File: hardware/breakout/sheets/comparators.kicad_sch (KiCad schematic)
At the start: 16 parts, among them U54 LM339, U55 MCP4728

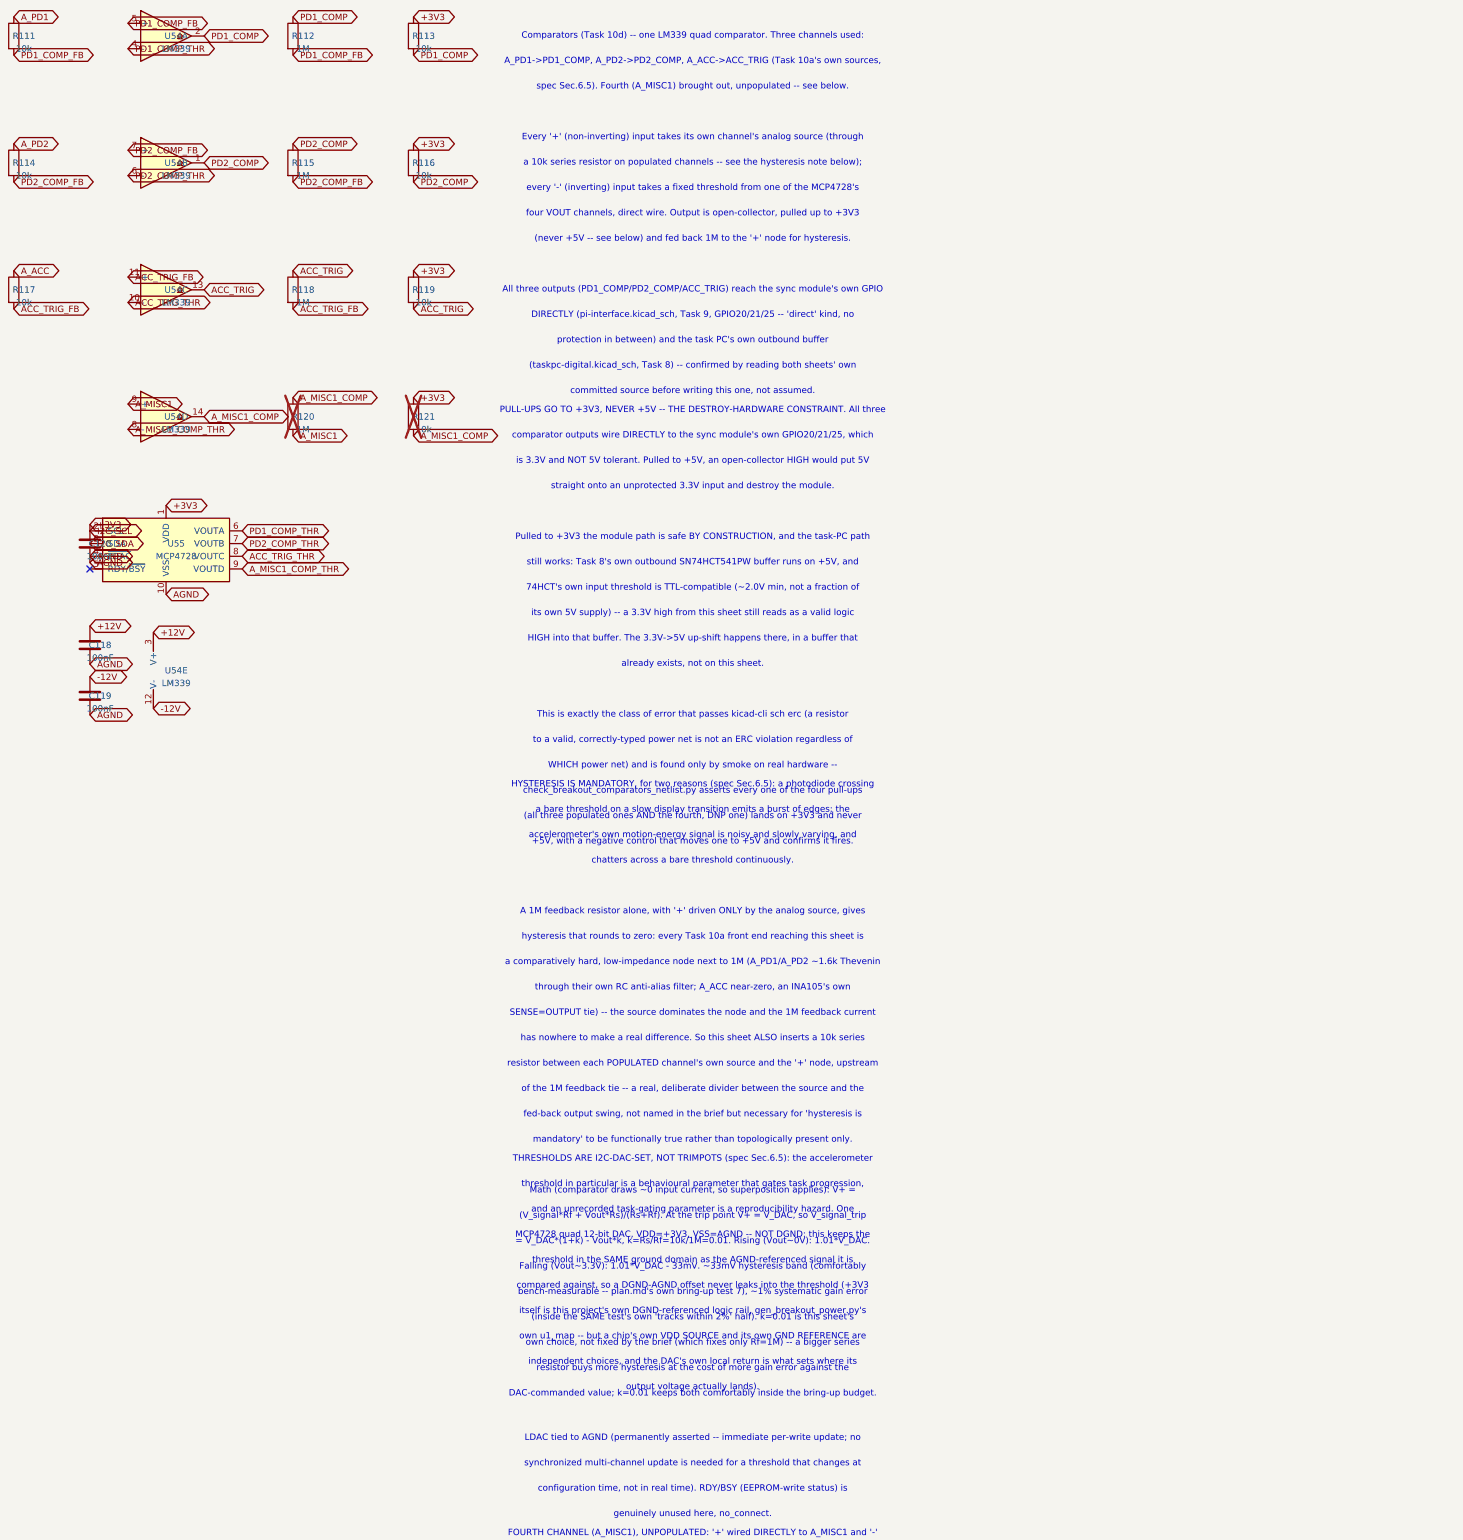
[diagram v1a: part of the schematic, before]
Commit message: fix(hw): run the LM339 from +12V and AGND, never -12V
LM339 pin 12 is labelled "V-"/negative supply, but it is also the common
emitter of all four open-collector output transistors. Whatever pin 12
sits on IS this sheet's output LOW level. On -12V an output LOW is
V- + V_CEsat ~ -11.9V, not 0V, and it genuinely settles there: a 10k
pull-up to +3V3 sources ~0.33mA against a ~16mA sink, so the transistor
stays hard in saturation.

PD1_COMP, PD2_COMP, ACC_TRIG and A_MISC1_COMP carried that level with no
series resistance and no clamp anywhere on the path:

  - J7 pins 38/40/22 (GPIO20/21/25), pad absolute minimum -0.5V. -11.9V
    forward-biases the module's substrate diode at ~1.5mA continuous.
  - U11 pins 2/3/4, SN74HCT541 inputs, absolute minimum -0.5V likewise.
  - U61 pins 6/8, ACSL-6400 LED cathodes with anodes on +5V through 430R:
    I_F ~ 36mA against a 20mA absolute maximum.

It also corrupted the hysteresis silently. The ~33mV band is derived from
a 0->3.3V output swing; the real swing was 15.2V, giving ~150mV and a
~118mV offset from the commanded threshold -- 12% at V_DAC = 1V, against
a 2% bring-up acceptance criterion.

V- = AGND costs nothing. The MCP4728 that sets every threshold is on
+3V3, so thresholds are 0-3.3V; all three populated channels' sources are
AGND-referenced and unipolar-positive; and V+ = +12V still puts the input
common-mode ceiling (10.5V) above anything the front end delivers. The
sheet no longer consumes -12V at all, so its second decoupler moves to
+12V/AGND with it (33/33 -> 34/32 on the power sheet's rail-pair table).
Both decouplers are kept rather than collapsed to one so no reference
designator and no BOM quantity changes, leaving Task 13's committed BOM
and procurement audit valid.

The one caveat, on-sheet as note 6 and in the generator docstring:
A_MISC1 is the only +-5V-capable input reaching this sheet and it is the
DNP fourth channel's '+' source. With V- = AGND that channel can no
longer threshold its input's negative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
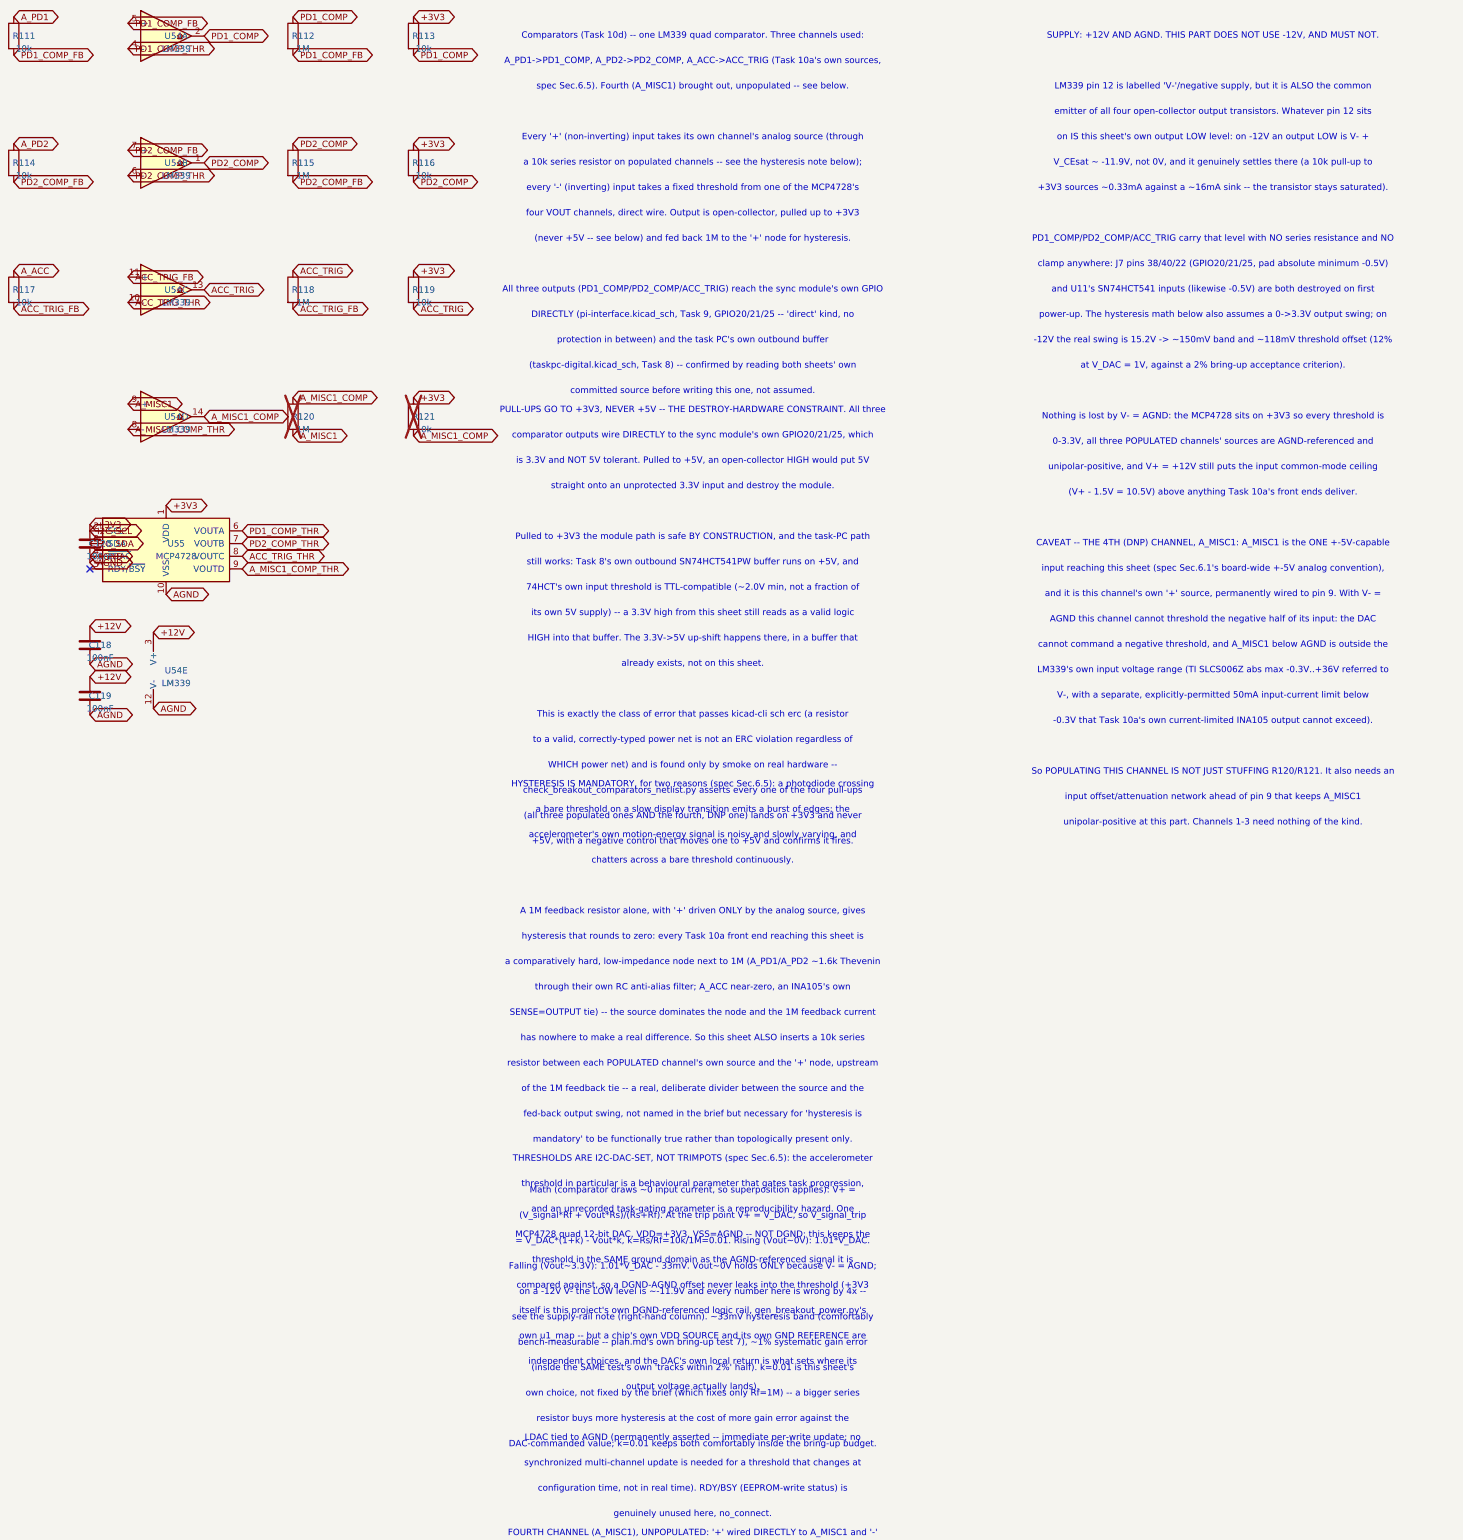
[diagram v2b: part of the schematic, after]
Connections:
- net +12V: now also C119.1
- net AGND: now also U54.12 (V-)
- removed net -12V: C119.1, U54.12 (V-)
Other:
- note added: "(V+ - 1.5V = 10.5V) above anything Task 10a's front ends deliver."
- note added: "+3V3 sources ~0.33mA against a ~16mA sink -- the transistor stays saturated)."
- note added: "-0.3V that Task 10a's own current-limited INA105 output cannot exceed)."
- note added: "-12V the real swing is 15.2V -> ~150mV band and ~118mV threshold offset (12%"
- note added: "0-3.3V, all three POPULATED channels' sources are AGND-referenced and"
- note added: "AGND this channel cannot threshold the negative half of its input: the DAC"
- note added: "CAVEAT -- THE 4TH (DNP) CHANNEL, A_MISC1: A_MISC1 is the ONE +-5V-capable"
- note added: "Falling (Vout~3.3V): 1.01*V_DAC - 33mV. Vout~0V holds ONLY because V- = AGND;"
- note added: "LM339 pin 12 is labelled 'V-'/negative supply, but it is ALSO the common"
- note added: "LM339's own input voltage range (TI SLCS006Z abs max -0.3V..+36V referred to"
- note added: "Nothing is lost by V- = AGND: the MCP4728 sits on +3V3 so every threshold is"
- note added: "PD1_COMP/PD2_COMP/ACC_TRIG carry that level with NO series resistance and NO"
- note added: "SUPPLY: +12V AND AGND. THIS PART DOES NOT USE -12V, AND MUST NOT."
- note added: "So POPULATING THIS CHANNEL IS NOT JUST STUFFING R120/R121. It also needs an"
- note added: "V-, with a separate, explicitly-permitted 50mA input-current limit below"
- note added: "V_CEsat ~ -11.9V, not 0V, and it genuinely settles there (a 10k pull-up to"
- note added: "and U11's SN74HCT541 inputs (likewise -0.5V) are both destroyed on first"
- note added: "and it is this channel's own '+' source, permanently wired to pin 9. With V- ="
- note added: "at V_DAC = 1V, against a 2% bring-up acceptance criterion)."
- note added: "cannot command a negative threshold, and A_MISC1 below AGND is outside the"
- note added: "clamp anywhere: J7 pins 38/40/22 (GPIO20/21/25, pad absolute minimum -0.5V)"
- note added: "emitter of all four open-collector output transistors. Whatever pin 12 sits"
- note added: "input offset/attenuation network ahead of pin 9 that keeps A_MISC1"
- note added: "input reaching this sheet (spec Sec.6.1's board-wide +-5V analog convention),"
- note added: "on IS this sheet's own output LOW level: on -12V an output LOW is V- +"
- note added: "on a -12V V- the LOW level is ~-11.9V and every number here is wrong by 4x --"
- note added: "power-up. The hysteresis math below also assumes a 0->3.3V output swing; on"
- note added: "see the supply-rail note (right-hand column). ~33mV hysteresis band (comfortably"
- note added: "unipolar-positive at this part. Channels 1-3 need nothing of the kind."
- note added: "unipolar-positive, and V+ = +12V still puts the input common-mode ceiling"
- note removed: "Falling (Vout~3.3V): 1.01*V_DAC - 33mV. ~33mV hysteresis band (comfortably"

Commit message: fix(hw): protect comparator channel 4's live A_MISC1 input with a series R
A_MISC1 is a live +-5V net (U28's INA105 output), permanently wired to
U54 pin 9 regardless of this channel's own populate state, and also
fanned out to U34/U36 and every ADG1206 mux's own S14. With V- = AGND
(the prior round's own fix), A_MISC1's negative half sits outside the
LM339's input range on every assembled board -- a bare wire from pin 9
is a standing clamp at the input protection diode's forward drop, with
fault current limited only by the INA105's own current limit, straight
into the LM339's substrate. Channels 1-3 are protected by R111/R114/R117
(10k series); channel 4 had no equivalent.

R190 (10k, populated -- not DNP, unlike this channel's pull-up/feedback)
closes that gap, wired identically to channels 1-3: A_MISC1 -> R190 ->
A_MISC1_COMP_FB -> U54 pin 9. It does not populate the channel in the
sense that matters for thresholding (feedback and pull-up stay DNP), it
only bounds the fault current to ~0.43mA instead of a bare wire.

A prior attempt deferred this because an auto-numbered resistor becomes
comparators.kicad_sch's own new "R" maximum, and opto-ni/opto-intan/
control-usb-i2c all seed their own resistor numbering from it via
find_max_refs(COMPARATORS_SCH) -- renumbering ~66 already-committed
refdes for no functional reason. R190 is placed with an explicit refdes
(two_pin()'s own new `ref=` passthrough, bypassing sch.next_ref("R"))
chosen to sit above the whole board's prior "R" range (189) on purpose,
and the three downstream generators pin their own inherited "R" seed to
its pre-R190 value (121/170/187) rather than re-deriving it from this
sheet's text. Confirmed by regenerating all three in-memory and diffing
their own (ref -> value) map against the committed sheets: zero refs
added, removed, or changed. Diffing the whole board's own component
list (netlist-contract.json) against 52dfcf7 confirms the same at the
board level -- R190 added, nothing else touched.

chec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
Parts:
- added R190: 10k, Resistor_SMD:R_0603_1608Metric, symbol Device:R
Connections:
- net A_MISC1: now also R190.1; no longer R120.2, U54.9 (+)
- new net A_MISC1_COMP_FB: R120.2, R190.2, U54.9 (+)
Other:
- note added: "'-' wired directly to the DAC's own VOUTD -- both real, permanent connections"
- note added: "-0.3V that Task 10a's own current-limited INA105 output cannot exceed). R190"
- note added: "DNP feedback and pull-up still need stuffing, AND (module docstring / note 6)"
- note added: "FOURTH CHANNEL (A_MISC1): '+' reaches A_MISC1 through R190 (10k, POPULATED),"
- note added: "R190 (10k, POPULATED -- see the fourth-channel note, left column). With V- ="
- note added: "R190 IS POPULATED, UNLIKE THE PULL-UP/FEEDBACK, BECAUSE A_MISC1 IS LIVE: it is"
- note added: "R190 does not by itself make this channel a working threshold comparator: the"
- note added: "V- = AGND (see the supply-rail note, right-hand column), A_MISC1's negative"
- note added: "already there, it does not populate the channel."
- note added: "already-committed resistors -- see CHANNEL4_SERIES_REF's own comment."
- note added: "an input offset/attenuation network ahead of pin 9 keeping A_MISC1 unipolar-"
- note added: "analog-frontend.kicad_sch's own INA105 (U28) output, permanently wired here and"
- note added: "and it is this channel's own '+' source, permanently wired to pin 9 through"
- note added: "both already stuffed for the other 3 channels). Only the pull-up (10k) and the"
- note added: "bounds the resulting fault current to ~0.43mA instead of leaving pin 9 a bare"
- note added: "bounds the resulting fault current to ~0.43mA on every assembled board; it"
- note added: "does not widen the LM339's own input range, which stays a real limit."
- note added: "exactly (same value, same role); its own refdes is minted out of band (not"
- note added: "half sits outside the LM339's own input range on every assembled board -- R190"
- note added: "hysteresis feedback (1M) are DNP -- real land patterns on the PCB (populating"
- note added: "positive at this part -- R190 protects the part from the live net that is"
- note added: "regardless of what else here is populated (the LM339 and MCP4728 packages are"
- note added: "sch.next_ref) specifically so it does not renumber opto-ni/opto-intan's own"
- note added: "them later is an assembly step, not a respin), just not stuffed by default."
- note added: "to every ADG1206 mux's own S14, whether or not this channel is ever used. With"
- note added: "wire into the input protection diode. Matches R111/R114/R117 on channels 1-3"
- note removed: "(10k) and the hysteresis feedback (1M) are DNP -- real land patterns on the"
- note removed: "-0.3V that Task 10a's own current-limited INA105 output cannot exceed)."
- note removed: "FOURTH CHANNEL (A_MISC1), UNPOPULATED: '+' wired DIRECTLY to A_MISC1 and '-'"
- note removed: "No series resistor is placed for this channel, unlike channels 1-3: with the"
- note removed: "PCB (populating them later is an assembly step, not a respin), just not"
- note removed: "and it is this channel's own '+' source, permanently wired to pin 9. With V- ="
- note removed: "channel, not a defect carried into the three primary ones."
- note removed: "connections regardless of what else here is populated (the LM339 and MCP4728"
- note removed: "deliberate divider (A_MISC1's own source impedance, Task 10a's INA105 output,"
- note removed: "directly to the DAC's own VOUTD -- both real, permanent, never-floating"
- note removed: "feedback resistor ALSO DNP by default, a populated-but-orphaned series resistor"
- note removed: "have been). A documented simplification for a secondary 'populate option'"
- note removed: "is ever fully populated, somewhat less hysteresis than channels 1-3's own"
- note removed: "is near zero, same reasoning as channels 1-3's own un-augmented '+' node would"
- note removed: "packages are both already stuffed for the other 3 channels). Only the pull-up"
- note removed: "simpler and safer to wire '+' straight to A_MISC1 and accept, if this channel"
- note removed: "stuffed by default."
- note removed: "would only float the '+' input the moment someone stuffed the feedback alone --"
